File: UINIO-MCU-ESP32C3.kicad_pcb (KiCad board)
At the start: 2 copper layers, 59.8 x 20.4 mm, 50 parts, among them J1 Conn_01x15_Male, J2 外接串行下载接口, J3 Conn_01x15_Male, SW1 复位按键, SW2 下载按键, U1 ME6211C33M5G-N, U2 W25Q128JVSSIQ, U3 ESP32-C3, U4 CH343P, Y1 40MHz

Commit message: Release UINIO-MCU-ESP32C3 version 3.0.0.
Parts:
- moved C1 0.22 mm to (146.2, 103.0)

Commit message: Release UINIO-MCU-ESP32C3 version 3.0.0.
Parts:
- moved ? 0.06 mm to (141.7, 103.1)
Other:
- board text added: "ADC1 IO4/SDA"
- board text added: "ADC2 IO5/SCL"
- board text removed: "ADC1 IO4 SDA"
- board text removed: "ADC2 IO5 SCL"

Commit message: Release UINIO-MCU-ESP32C3 version 3.1.0.
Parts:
- added R3: 5.1K, Resistor_SMD:R_0402_1005Metric, F.Cu at (139.7, 106.7)
- added R8: 5.1K, Resistor_SMD:R_0402_1005Metric, F.Cu at (139.7, 104.9)
- moved R6 1.64 mm to (139.7, 103.1)
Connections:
- USB1 pad A5: unconnected-(USB1-PadA5) -> Net-(R3-Pad1)
- USB1 pad B5: unconnected-(USB1-PadB5) -> Net-(R8-Pad1)
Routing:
- net GND: track 223.3 -> 244.4 mm, vias 102 -> 110
- net Net-(R3-Pad1): track 0.00 -> 16.0 mm, vias 0 -> 4
- net Net-(R8-Pad1): track 0.00 -> 12.5 mm, vias 0 -> 2
- net Net-(R6-Pad2): track 8.08 -> 6.42 mm
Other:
- board text added: "Version 3.1.0"
- board text removed: "Version 3.0.0"

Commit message: Fix bug.
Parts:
- moved C9 0.42 mm to (164.4, 98.2)
- moved C7 0.35 mm to (167.6, 98.2)
- moved C4 0.34 mm to (165.5, 98.2)
- moved C5 0.31 mm to (166.6, 98.2)
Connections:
- J1 pad 7: /GPIO5/ADC2/SCL -> /GPIO4/ADC1/SDA
- J1 pad 8: /GPIO4/ADC1/SDA -> /GPIO5/ADC2/SCL
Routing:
- net /GPIO4/ADC1/SDA: track 11.7 -> 8.44 mm
- net /GPIO5/ADC2/SCL: track 9.00 -> 10.8 mm, vias 1 -> 0
- net /CHIP_EN: track 32.6 -> 31.8 mm
- net /VDD_3.3V: track 147.0 -> 147.7 mm
- net GND: track 244.4 -> 244.8 mm, vias 110 -> 109
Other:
- board text added: "IO0"
- board text added: "IO1"
- board text removed: "RXD1"
- board text removed: "TXD1"

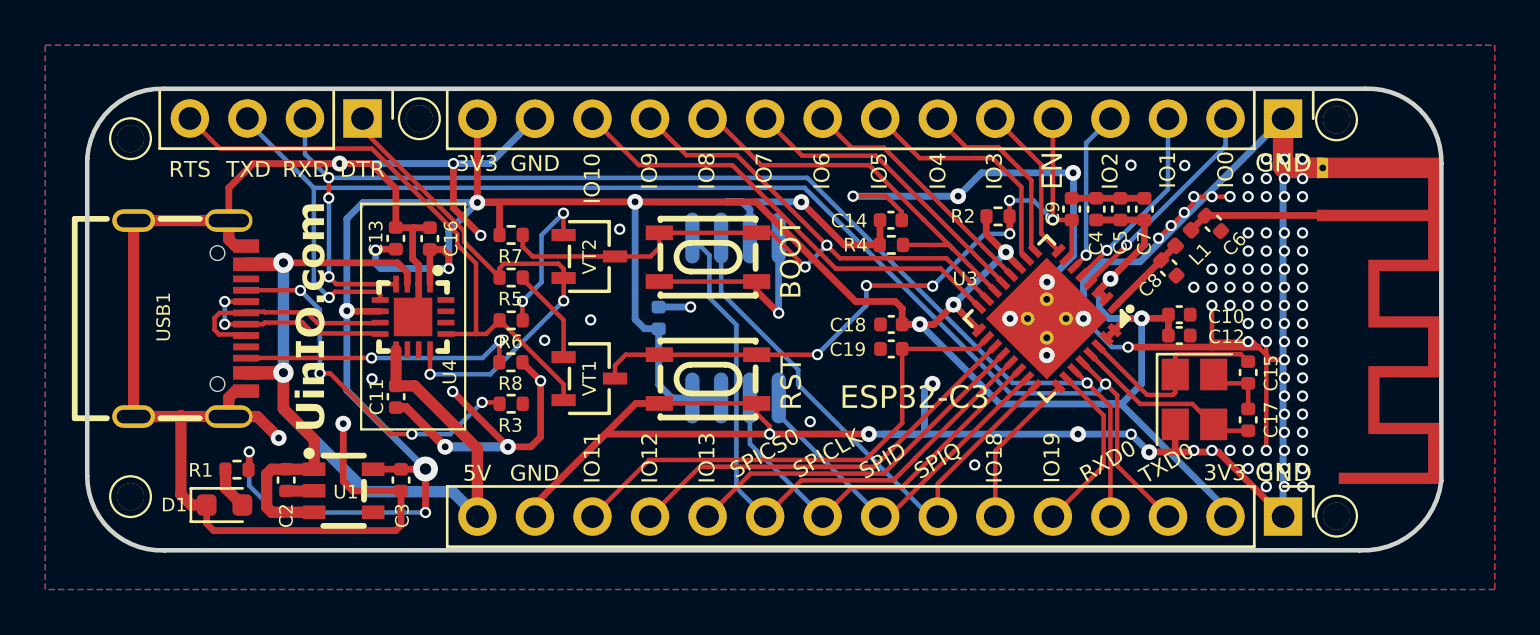
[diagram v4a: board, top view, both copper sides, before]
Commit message: Release UINIO-MCU-ESP32C3 version 3.2.0.
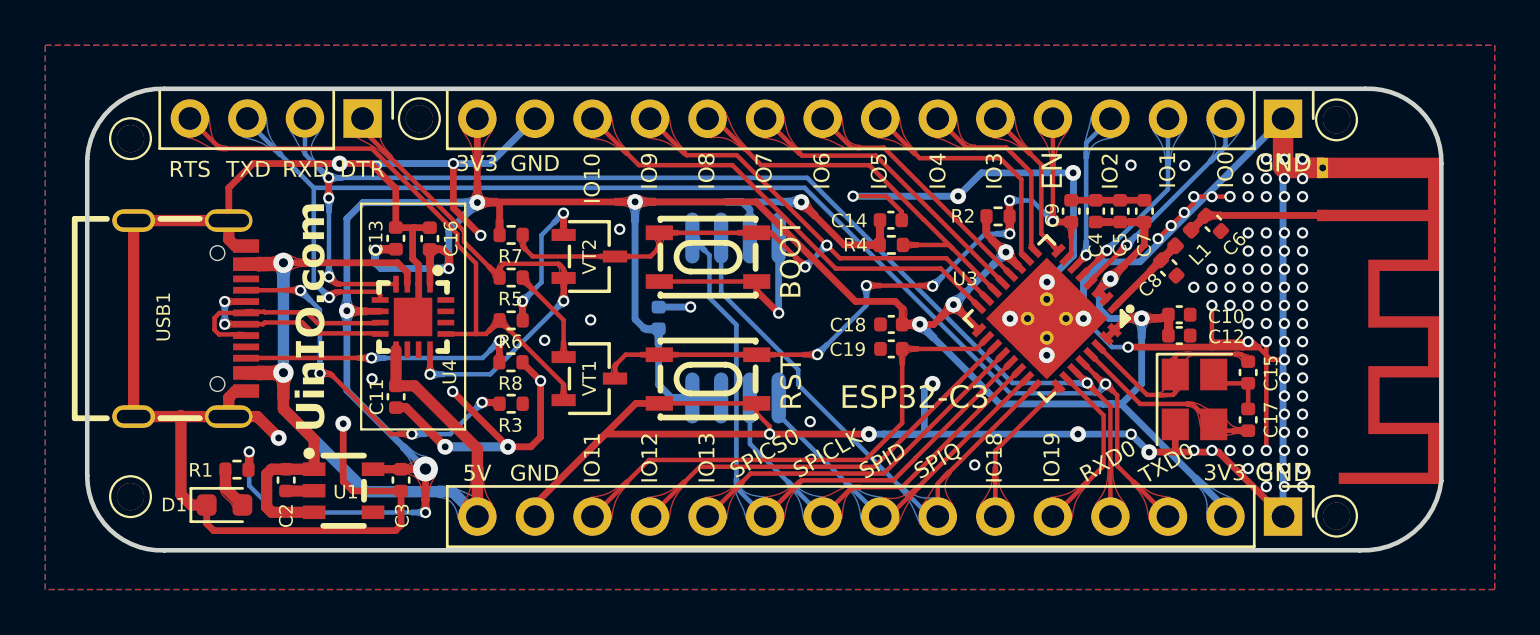
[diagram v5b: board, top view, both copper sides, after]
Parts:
- moved C4 0.09 mm to (165.5, 98.2)
- moved C9 0.09 mm to (164.4, 98.2)
- moved C5 0.09 mm to (166.6, 98.2)
- moved C7 0.09 mm to (167.6, 98.2)
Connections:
- net /GPIO0/U1TXD renamed /GPIO0
- net /GPIO1/U1RXD renamed /GPIO1
- net /GPIO4/ADC1/SDA renamed /GPIO4
- net /GPIO5/ADC2/SCL renamed /GPIO5
- net /GPIO8/PWM renamed /GPIO8
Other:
- board text added: "Version 3.2.0"
- board text removed: "ADC1 IO4/SDA"
- board text removed: "ADC2 IO5/SCL"
- board text removed: "CHIP_EN"
- board text removed: "IO0 TXD1"
- board text removed: "IO1 RXD1"
- board text removed: "IO11 VDD_SPI"
- board text removed: "IO12 SPIHD"
- board text removed: "IO13 SPIWP"
- board text removed: "IO18 USB_D-"
- board text removed: "IO19 USB_D+"
- board text removed: "IO8 PWM"
- board text removed: "IO9 BOOT"
- board text removed: "Version 3.1.0"

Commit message: Update PCB layout.
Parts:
- moved C9 0.08 mm to (164.4, 98.2)
- moved C4 0.08 mm to (165.5, 98.2)
- moved C5 0.08 mm to (166.6, 98.2)
- moved C7 0.08 mm to (167.6, 98.2)
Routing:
- net GND: track 244.8 -> 242.6 mm

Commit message: Update PCB.
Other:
- board text added: "G0"
- board text added: "G1"
- board text added: "G10"
- board text added: "G11"
- board text added: "G12"
- board text added: "G13"
- board text added: "G18"
- board text added: "G19"
- board text added: "G2"
- board text added: "G3"
- board text added: "G4"
- board text added: "G5"
- board text added: "G6"
- board text added: "G7"
- board text added: "G8"
- board text added: "G9"
- board text removed: "IO0"
- board text removed: "IO1"
- board text removed: "IO10"
- board text removed: "IO11"
- board text removed: "IO12"
- board text removed: "IO13"
- board text removed: "IO18"
- board text removed: "IO19"
- board text removed: "IO2"
- board text removed: "IO3"
- board text removed: "IO4"
- board text removed: "IO5"
- board text removed: "IO6"
- board text removed: "IO7"
- board text removed: "IO8"
- board text removed: "IO9"
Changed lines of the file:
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@@
     (effects (font (size 0.85 0.85) (thickness 0.2)) (justify mirror))
   )
-  (gr_text "IO1" (at 168.65 96.42 90) (layer "F.SilkS")
-    (effects (font (size 0.7 0.7) (thickness 0.15)))
+  (gr_text "G1" (at 168.66 96.38 90) (layer "F.SilkS")
+    (effects (font (size 0.8 0.8) (thickness 0.15)))
   )
   (gr_text "TXD" (at 128.08 96.4) (layer "F.SilkS")
     (effects (font (size 0.7 0.7) (thickness 0.15)))
   )
-  (gr_text "3V3" (at 171.16 109.79) (layer "F.SilkS")
-    (effects (font (size 0.7 0.7) (thickness 0.15)))
-  )
-  (gr_text "SPICLK" (at 153.63 108.94 30) (layer "F.SilkS")
-    (effects (font (size 0.7 0.7) (thickness 0.15)))
-  )
-  (gr_text "IO19" (at 163.54 109.12 90) (layer "F.SilkS")
-    (effects (font (size 0.7 0.7) (thickness 0.15)))
+  (gr_text "3V3" (at 171.16 109.8405) (layer "F.SilkS")
+    (effects (font (size 0.7 0.7) (thickness 0.15)))
+  )
+  (gr_text "SPICLK" (at 153.73 108.94 30) (layer "F.SilkS")
+    (effects (font (size 0.7 0.7) (thickness 0.15)))
+  )
+  (gr_text "G19" (at 163.61 109.13 90) (layer "F.SilkS")
+    (effects (font (size 0.8 0.8) (thickness 0.15)))
   )
   (gr_text "ESP32-C3" (at 157.48 106.46) (layer "F.SilkS")
@@
     (effects (font (size 0.7 0.7) (thickness 0.15)))
   )
-  (gr_text "IO8" (at 148.31 96.47 90) (layer "F.SilkS")
-    (effects (font (size 0.7 0.7) (thickness 0.15)))
-  )
-  (gr_text "EN" (at 163.56 96.45 90) (layer "F.SilkS")
-    (effects (font (size 0.9 0.9) (thickness 0.15)))
-  )
-  (gr_text "IO11\n" (at 143.25 109.13 90) (layer "F.SilkS")
-    (effects (font (size 0.7 0.7) (thickness 0.15)))
-  )
-  (gr_text "IO6" (at 153.39 96.47 90) (layer "F.SilkS")
-    (effects (font (size 0.7 0.7) (thickness 0.15)))
+  (gr_text "G8" (at 148.351428 96.38 90) (layer "F.SilkS")
+    (effects (font (size 0.8 0.8) (thickness 0.15)))
+  )
+  (gr_text "EN" (at 163.56 96.38 90) (layer "F.SilkS")
+    (effects (font (size 0.8 0.8) (thickness 0.15)))
+  )
+  (gr_text "G11\n" (at 143.27 109.13 90) (layer "F.SilkS")
+    (effects (font (size 0.8 0.8) (thickness 0.15)))
+  )
+  (gr_text "G6" (at 153.422856 96.38 90) (layer "F.SilkS")
+    (effects (font (size 0.8 0.8) (thickness 0.15)))
   )
   (gr_text "GND\n" (at 140.73 96.14) (layer "F.SilkS")
     (effects (font (size 0.7 0.7) (thickness 0.15)))
   )
-  (gr_text "IO2" (at 166.11 96.47 90) (layer "F.SilkS")
-    (effects (font (size 0.7 0.7) (thickness 0.15)))
-  )
-  (gr_text "IO13\n" (at 148.315 109.13 90) (layer "F.SilkS")
-    (effects (font (size 0.7 0.7) (thickness 0.15)))
-  )
-  (gr_text "SPID" (at 156.07 109.26 30) (layer "F.SilkS")
-    (effects (font (size 0.7 0.7) (thickness 0.15)))
-  )
-  (gr_text "RXD0" (at 166.01 109.278334 30) (layer "F.SilkS")
-    (effects (font (size 0.7 0.7) (thickness 0.15)))
-  )
-  (gr_text "IO0" (at 171.21 96.41 90) (layer "F.SilkS")
-    (effects (font (size 0.7 0.7) (thickness 0.15)))
-  )
-  (gr_text "IO3" (at 161 96.47 90) (layer "F.SilkS")
-    (effects (font (size 0.7 0.7) (thickness 0.15)))
-  )
-  (gr_text "IO12" (at 145.79 109.13 90) (layer "F.SilkS")
-    (effects (font (size 0.7 0.7) (thickness 0.15)))
+  (gr_text "G2" (at 166.11 96.38 90) (layer "F.SilkS")
+    (effects (font (size 0.8 0.8) (thickness 0.15)))
+  )
+  (gr_text "G13\n" (at 148.35 109.13 90) (layer "F.SilkS")
+    (effects (font (size 0.8 0.8) (thickness 0.15)))
+  )
+  (gr_text "SPID" (at 156.09 109.26 30) (layer "F.SilkS")
+    (effects (font (size 0.7 0.7) (thickness 0.15)))
+  )
+  (gr_text "RXD0" (at 166.01 109.328334 30) (layer "F.SilkS")
+    (effects (font (size 0.7 0.7) (thickness 0.15)))
+  )
+  (gr_text "G0" (at 171.21 96.38 90) (layer "F.SilkS")
+    (effects (font (size 0.8 0.8) (thickness 0.15)))
+  )
+  (gr_text "G3" (at 161.03 96.38 90) (layer "F.SilkS")
+    (effects (font (size 0.8 0.8) (thickness 0.15)))
+  )
+  (gr_text "G12" (at 145.81 109.13 90) (layer "F.SilkS")
+    (effects (font (size 0.8 0.8) (thickness 0.15)))
   )
   (gr_text "RTS" (at 125.49 96.4) (layer "F.SilkS")
     (effects (font (size 0.7 0.7) (thickness 0.15)))
   )
-  (gr_text "GND\n" (at 173.76 96.12) (layer "F.SilkS")
-    (effects (font (size 0.8 0.8) (thickness 0.15)))
+  (gr_text "GND\n" (at 173.76 96.200047) (layer "F.SilkS")
+    (effects (font (size 0.7 0.7) (thickness 0.15)))
   )
   (gr_text "3V3" (at 138.17 96.14) (layer "F.SilkS")
     (effects (font (size 0.7 0.7) (thickness 0.15)))
   )
-  (gr_text "IO18" (at 161 109.13 90) (layer "F.SilkS")
-    (effects (font (size 0.7 0.7) (thickness 0.15)))
+  (gr_text "G18" (at 161.07 109.13 90) (layer "F.SilkS")
+    (effects (font (size 0.8 0.8) (thickness 0.15)))
   )
   (gr_text "RST" (at 152.04 105.84 90) (layer "F.SilkS")
@@
     (effects (font (size 0.7 0.7) (thickness 0.15)))
   )
-  (gr_text "GND\n" (at 173.76 109.78) (layer "F.SilkS")
-    (effects (font (size 0.8 0.8) (thickness 0.15)))
-  )
-  (gr_text "IO5" (at 155.92 96.47 90) (layer "F.SilkS")
-    (effects (font (size 0.7 0.7) (thickness 0.15)))
-  )
-  (gr_text "IO9" (at 145.78 96.47 90) (layer "F.SilkS")
-    (effects (font (size 0.7 0.7) (thickness 0.15)))
-  )
-  (gr_text "IO4" (at 158.51 96.47 90) (layer "F.SilkS")
-    (effects (font (size 0.7 0.7) (thickness 0.15)))
-  )
-  (gr_text "SPICS0" (at 150.86 108.928734 30) (layer "F.SilkS")
+  (gr_text "GND\n" (at 173.76 109.8405) (layer "F.SilkS")
+    (effects (font (size 0.7 0.7) (thickness 0.15)))
+  )
+  (gr_text "G5" (at 155.95857 96.38 90) (layer "F.SilkS")
+    (effects (font (size 0.8 0.8) (thickness 0.15)))
+  )
+  (gr_text "G9" (at 145.815714 96.38 90) (layer "F.SilkS")
+    (effects (font (size 0.8 0.8) (thickness 0.15)))
+  )
+  (gr_text "G4" (at 158.494284 96.38 90) (layer "F.SilkS")
+    (effects (font (size 0.8 0.8) (thickness 0.15)))
+  )
+  (gr_text "SPICS0" (at 150.98 108.94 30) (layer "F.SilkS")
     (effects (font (size 0.7 0.7) (thickness 0.15)))
   )
@@
     (effects (font (size 0.9 0.9) (thickness 0.2)))
   )
-  (gr_text "IO10" (at 143.25 96.803333 90) (layer "F.SilkS")
-    (effects (font (size 0.7 0.7) (thickness 0.15)))
+  (gr_text "G10" (at 143.28 96.760952 90) (layer "F.SilkS")
+    (effects (font (size 0.8 0.8) (thickness 0.15)))
   )
   (gr_text "5V" (at 138.17 109.809) (layer "F.SilkS")
     (effects (font (size 0.7 0.7) (thickness 0.15)))
   )
-  (gr_text "IO7" (at 150.84 96.47 90) (layer "F.SilkS")
-    (effects (font (size 0.7 0.7) (thickness 0.15)))
+  (gr_text "G7" (at 150.887142 96.38 90) (layer "F.SilkS")
+    (effects (font (size 0.8 0.8) (thickness 0.15)))
   )
   (gr_text "SPIQ" (at 158.5 109.253734 30) (layer "F.SilkS")
@@
   (segment (start 172.2 104) (end 172.41 104) (width 0.2) (layer "F.Cu") (net 2))
   (segment (start 135.37 98.97) (end 135.32 99.02) (width 0.3) (layer "F.Cu") (net 2))
-  (segment (start 169.8 97.6) (end 169.8 97.88) (width 0.2) (layer "F.Cu") (net 2))
   (segment (start 145.715 106.725) (end 145.175 106.725) (width 0.3) (layer "F.Cu") (net 2))
   (segment (start 128.28 96.14) (end 127.209 97.211) (width 0.3) (layer "F.Cu") (net 2))
@@
   (segment (start 127.209 98.655) (end 127.209 99.493982) (width 0.5) (layer "F.Cu") (net 2))
   (segment (start 175.49 96.33) (end 173.8 96.33) (width 0.9) (layer "F.Cu") (net 2))
+  (segment (start 169.77 97.6) (end 169.38 97.99) (width 0.2) (layer "F.Cu") (net 2))
+  (segment (start 169.38 97.99) (end 169.38 98.3) (width 0.2) (layer "F.Cu") (net 2))
   (segment (start 150.51 106.725) (end 146.21 106.725) (width 0.2) (layer "F.Cu") (net 2))
+  (segment (start 169.8 97.6) (end 169.77 97.6) (width 0.2) (layer "F.Cu") (net 2))
   (segment (start 172.2 106.97) (end 172.2 105.84) (width 0.2) (layer "F.Cu") (net 2))
   (segment (start 127.971 106.18) (end 127.495018 106.18) (width 0.5) (layer "F.Cu") (net 2))
@@
   (segment (start 170.59 104.24) (end 171.96 104.24) (width 0.3) (layer "F.Cu") (net 2))
   (segment (start 171.96 104.24) (end 172.2 104) (width 0.2) (layer "F.Cu") (net 2))
-  (segment (start 169.8 97.88) (end 169.38 98.3) (width 0.2) (layer "F.Cu") (net 2))
   (segment (start 172.67 104.26) (end 173.21 104.8) (width 0.2) (layer "F.Cu") (net 2))
   (segment (start 125.095 110.755) (end 125.55 111.21) (width 0.5) (layer "F.Cu") (net 2))

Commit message: PCB Update.
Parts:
- J1, J3: value Conn_01x15_Male -> Conn_01x15_Pin; moved to B.Cu
- J2: value 外接串行下载接口 -> Conn_01x04_Pin
- moved C4 0.15 mm to (165.5, 98.0)
- moved C5 0.15 mm to (166.6, 98.0)
- moved C7 0.15 mm to (167.6, 98.0)
- moved C9 0.15 mm to (164.4, 98.0)
- turned J1 to 90 degrees
- turned J3 to 90 degrees
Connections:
- J2 pad 2: /U0RXD -> /U0TXD
- J2 pad 3: /U0TXD -> /U0RXD
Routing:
- net /U0RXD: track 54.9 -> 57.9 mm, vias 4 -> 5
- net /U0TXD: track 59.2 -> 58.7 mm
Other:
- board text added: "Version 3.3.0"
- board text added: "可选"
- board text removed: "Version 3.2.0"
